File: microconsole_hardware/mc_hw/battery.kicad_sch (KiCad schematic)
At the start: 25 parts, among them J2 USB_C_Receptacle, Q1 DMP2035U-7, Q2 DMP2035U-7, SW19 SPDT_Slide_PTH_11.6x4.0mm, U1 MCP73833-FCI/UN, U2 S2B-PH-K-S

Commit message: second cleanup
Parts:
- removed C1, C2: 10uF, project_parts:C_0805_2012Metric_KEMET_IPC-B, symbol Device:C
- added C26, C27: 1206ZD106KAT2A, project_parts:C1206, symbol project_parts:1206ZD106KAT2A
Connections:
- net BAT+: now also C27.2
- net GND: now also C26.1, C27.1
- net USB-VBUS: now also C26.2

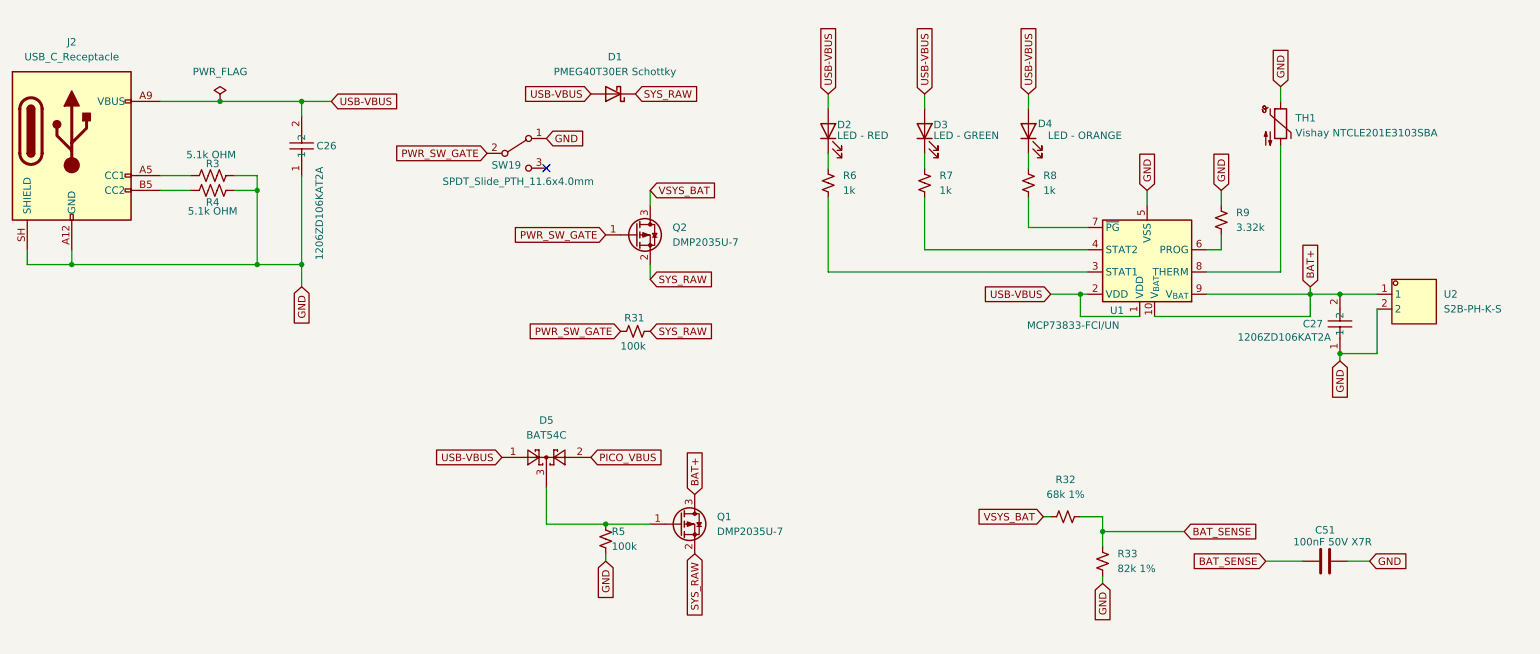
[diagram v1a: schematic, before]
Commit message: resistor and capacitor consolidation.
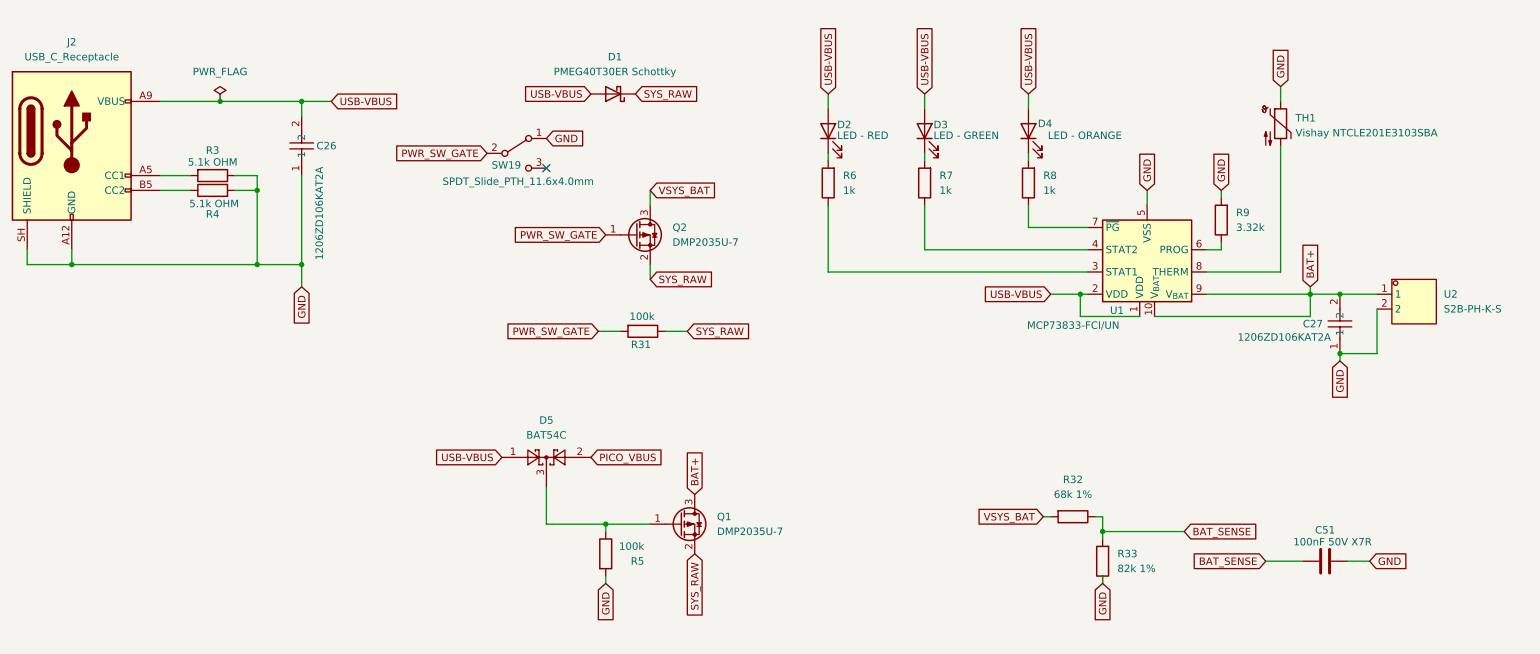
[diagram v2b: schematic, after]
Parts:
- R3, R4: footprint PCM_SparkFun-Resistor:R_0603_1608Metric -> Resistor_SMD:R_0603_1608Metric; symbol PCM_SparkFun-Resistor:R -> Device:R
- R31, R32, R33, R5, R6, R7, R8, R9: footprint PCM_SparkFun-Resistor:R_0603_1608Metric -> Resistor_SMD:R_0603_1608Metric; symbol PCM_SparkFun-Resistor:0.47_0603 -> Device:R
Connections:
- net GND: now also R3.1, R4.2; no longer R3.2, R4.1
- net at J2.A5 (CC1): now also R3.2; no longer R3.1
- net at J2.B5 (CC2): now also R4.1; no longer R4.2

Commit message: cleanup caps and resistors
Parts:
- R3, R4: value 5.1k OHM -> 5.1k
- R32: value 68k 1% -> 68k
- R33: value 82k 1% -> 82k
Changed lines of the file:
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@@
 			)
 		)
-		(property "Value" "68k 1%"
+		(property "Value" "68k"
 			(at 199.39 106.68 90)
 			(show_name no)
@@
 			)
 		)
-		(property "Value" "5.1k OHM"
+		(property "Value" "5.1k"
 			(at 52.07 49.784 90)
 			(show_name no)
@@
 			)
 		)
-		(property "Value" "5.1k OHM"
+		(property "Value" "5.1k"
 			(at 52.324 56.896 90)
 			(show_name no)
@@
 			)
 		)
-		(property "Value" "82k 1%"
+		(property "Value" "82k"
 			(at 207.01 119.3799 0)
 			(show_name no)

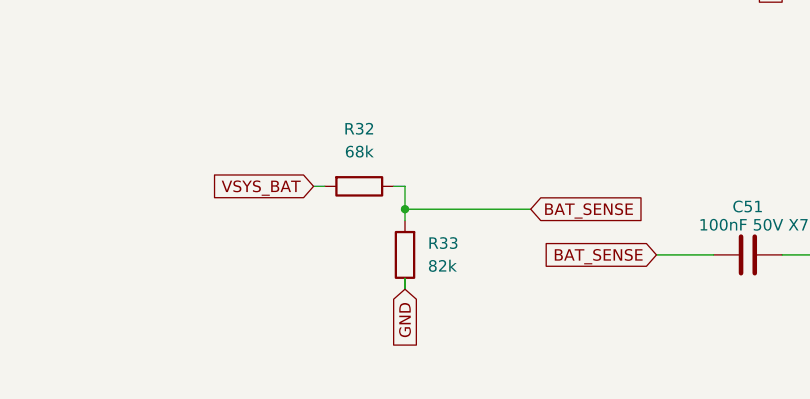
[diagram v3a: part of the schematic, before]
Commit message: cleanup ic symbol pin types
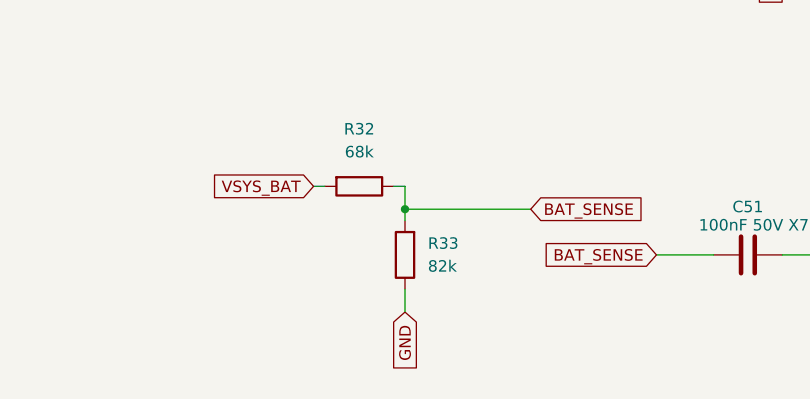
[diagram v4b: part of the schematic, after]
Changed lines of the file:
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@@
+	)
+	(junction
+		(at 204.47 113.03)
+		(diameter 0)
+		(color 0 0 0 0)
 	)
 	(junction
@@
 		(color 0 0 0 0)
 	)
-	(junction
-		(at 204.47 113.03)
-		(diameter 0)
-		(color 0 0 0 0)
-	)
 	(no_connect
 		(at 109.22 50.8)
@@
 	(wire
 		(pts
-			(xy 204.47 121.92) (xy 204.47 120.65)
-		)
-		(stroke
-			(width 0)
-			(type default)
-		)
-	)
-	(wire
-		(pts
 			(xy 173.99 49.53) (xy 173.99 48.26)
 		)
@@
 	(wire
 		(pts
+			(xy 204.47 113.03) (xy 218.44 113.03)
+		)
+		(stroke
+			(width 0)
+			(type default)
+		)
+	)
+	(wire
+		(pts
 			(xy 191.77 60.96) (xy 201.93 60.96)
 		)
@@
 	(wire
 		(pts
-			(xy 204.47 113.03) (xy 218.44 113.03)
-		)
-		(stroke
-			(width 0)
-			(type default)
-		)
-	)
-	(wire
-		(pts
 			(xy 232.41 118.11) (xy 238.76 118.11)
 		)
@@
 	(wire
 		(pts
+			(xy 204.47 113.03) (xy 204.47 114.3)
+		)
+		(stroke
+			(width 0)
+			(type default)
+		)
+	)
+	(wire
+		(pts
 			(xy 245.11 72.39) (xy 251.46 72.39)
 		)
@@
 	(wire
 		(pts
+			(xy 204.47 124.46) (xy 204.47 121.92)
+		)
+		(stroke
+			(width 0)
+			(type default)
+		)
+	)
+	(wire
+		(pts
 			(xy 173.99 38.1) (xy 173.99 40.64)
 		)
@@
 	(wire
 		(pts
-			(xy 204.47 110.49) (xy 204.47 114.3)
+			(xy 204.47 110.49) (xy 204.47 113.03)
 		)
 		(stroke
@@
 	(global_label "GND"
 		(shape input)
-		(at 204.47 121.92 270)
+		(at 204.47 124.46 270)
 		(fields_autoplaced yes)
 		(effects
@@
 		)
 		(property "Intersheetrefs" "${INTERSHEET_REFS}"
-			(at 204.47 128.7757 90)
-			(hide yes)
-			(show_name no)
+			(at 204.47 131.3157 90)
+			(hide yes)
+			(show_name no)

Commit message: consolidate parts 1
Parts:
- D2: MPN (none) -> LTST-C190KRKT; Manufacturer (none) -> Lite-On Inc.
- D3: MPN (none) -> LTST-C190KGKT; Manufacturer (none) -> Lite-On Inc.
- D4: MPN (none) -> LTST-C190KFKT; Manufacturer (none) -> Lite-On Inc.
- Q1, Q2: footprint (none) -> Package_TO_SOT_SMD:SOT-23
- R3, R4: MPN (none) -> RC0603FR-075K1L; Manufacturer (none) -> YAGEO; Power (none) -> 0.1W; Tolerance (none) -> 1%
- R31, R5: MPN (none) -> RC0603FR-07100KL; Manufacturer (none) -> YAGEO; Power (none) -> 0.1W; Tolerance (none) -> 1%
- R32: MPN (none) -> RC0603FR-0768KL; Manufacturer (none) -> YAGEO; Power (none) -> 0.1W; Tolerance (none) -> 1%
- R33: MPN (none) -> RC0603FR-0782KL; Manufacturer (none) -> YAGEO; Power (none) -> 0.1W; Tolerance (none) -> 1%
- R6, R7, R8: MPN (none) -> RC0603FR-071KL; Manufacturer (none) -> YAGEO; Power (none) -> 0.1W; Tolerance (none) -> 1%
- R9: MPN (none) -> RC0603FR-073K32L; Manufacturer (none) -> YAGEO; Power (none) -> 0.1W; Tolerance (none) -> 1%

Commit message: smal fix
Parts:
- Q1, Q2: MPN (none) -> DMP2035U-7; Manufacturer (none) -> Diodes Incorporated
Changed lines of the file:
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@@
+			)
+		)
+		(property "MPN" "DMP2035U-7"
+			(at 132.08 111.76 0)
+			(hide yes)
+			(show_name no)
+			(do_not_autoplace no)
+			(effects
+				(font
+					(size 1.27 1.27)
+				)
+			)
+		)
+		(property "Manufacturer" "Diodes Incorporated"
+			(at 132.08 111.76 0)
+			(hide yes)
+			(show_name no)
+			(do_not_autoplace no)
+			(effects
+				(font
+					(size 1.27 1.27)
+				)
 			)
 		)
@@
 			(at 124.46 62.23 0)
 			(hide yes)
+			(show_name no)
+			(do_not_autoplace no)
+			(effects
+				(font
+					(size 1.27 1.27)
+				)
+			)
+		)
+		(property "MPN" "DMP2035U-7"
+			(at 124.46 62.23 0)
+			(hide yes)
+			(show_name no)
+			(do_not_autoplace no)
+			(effects
+				(font
+					(size 1.27 1.27)
+				)
+			)
+		)
+		(property "Manufacturer" "Diodes Incorporated"
+			(at 124.46 62.23 0)
+			(hide yes)

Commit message: second fix
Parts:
- D1: MPN (none) -> PMEG40T30ERX; Manufacturer (none) -> Nexperia
- D5: MPN (none) -> BAT54C-7-F; Manufacturer (none) -> Diodes Incorporated
- SW19: MPN (none) -> COM-00102; Manufacturer (none) -> SparkFun Electronics
- TH1: MPN (none) -> NTCLE201E3103SBA; Manufacturer (none) -> Vishay / BCcomponents
- U1: MPN (none) -> MCP73833-FCI/UN; Manufacturer (none) -> Microchip Technology
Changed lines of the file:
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@@
+			)
+		)
+		(property "MPN" "PMEG40T30ERX"
+			(at 120.65 38.1 0)
+			(hide yes)
+			(show_name no)
+			(do_not_autoplace no)
+			(effects
+				(font
+					(size 1.27 1.27)
+				)
+			)
+		)
+		(property "Manufacturer" "Nexperia"
+			(at 120.65 38.1 0)
+			(hide yes)
+			(show_name no)
+			(do_not_autoplace no)
+			(effects
+				(font
+					(size 1.27 1.27)
+				)
 			)
 		)
@@
 			)
 		)
+		(property "MPN" "MCP73833-FCI/UN"
+			(at 212.09 63.5 0)
+			(hide yes)
+			(show_name no)
+			(do_not_autoplace no)
+			(effects
+				(font
+					(size 1.27 1.27)
+				)
+			)
+		)
+		(property "Manufacturer" "Microchip Technology"
+			(at 212.09 63.5 0)
+			(hide yes)
+			(show_name no)
+			(do_not_autoplace no)
+			(effects
+				(font
+					(size 1.27 1.27)
+				)
+			)
+		)
 		(pin "6"
 		)
@@
 			)
 		)
+		(property "MPN" "COM-00102"
+			(at 104.14 48.26 0)
+			(hide yes)
+			(show_name no)
+			(do_not_autoplace no)
+			(effects
+				(font
+					(size 1.27 1.27)
+				)
+			)
+		)
+		(property "Manufacturer" "SparkFun Electronics"
+			(at 104.14 48.26 0)
+			(hide yes)
+			(show_name no)
+			(do_not_autoplace no)
+			(effects
+				(font
+					(size 1.27 1.27)
+				)
+			)
+		)
 		(pin "2"
 		)
@@
 			)
 		)
+		(property "MPN" "BAT54C-7-F"
+			(at 109.22 100.33 0)
+			(hide yes)
+			(show_name no)
+			(do_not_autoplace no)
+			(effects
+				(font
+					(size 1.27 1.27)
+				)
+			)
+		)
+		(property "Manufacturer" "Diodes Incorporated"
+			(at 109.22 100.33 0)
+			(hide yes)
+			(show_name no)
+			(do_not_autoplace no)
+			(effects
+				(font
+					(size 1.27 1.27)
+				)
+			)
+		)
 		(pin "2"
 		)
@@
 			(at 234.95 43.18 0)
 			(hide yes)
+			(show_name no)
+			(do_not_autoplace no)
+			(effects
+				(font
+					(size 1.27 1.27)
+				)
+			)
+		)
+		(property "MPN" "NTCLE201E3103SBA"
+			(at 234.95 43.18 0)
+			(hide yes)
+			(show_name no)
+			(do_not_autoplace no)
+			(effects
+				(font
+					(size 1.27 1.27)
+				)
+			)
+		)
+		(property "Manufacturer" "Vishay / BCcomponents"
+			(at 234.95 43.18 0)
+			(hide yes)

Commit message: bom cleanup
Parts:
- C26, C27: Tolerance (none) -> 10%; Voltage (none) -> 10V
- C51: Tolerance (none) -> 10%; Voltage (none) -> 50V
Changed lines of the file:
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@@
+			)
+		)
+		(property "Tolerance" "10%"
+			(at 242.57 118.11 90)
+			(hide yes)
+			(show_name no)
+			(do_not_autoplace no)
+			(effects
+				(font
+					(size 1.27 1.27)
+				)
+			)
+		)
+		(property "Voltage" "50V"
+			(at 242.57 118.11 90)
+			(hide yes)
+			(show_name no)
+			(do_not_autoplace no)
+			(effects
+				(font
+					(size 1.27 1.27)
+				)
 			)
 		)
@@
 			)
 		)
-		(property "Datasheet" "https://lcsc.com/product-detail/presales_AVX-1206ZD106KAT2A_C597553.html"
+		(property "Datasheet" ""
 			(at 255.27 77.47 0)
 			(hide yes)
@@
 		)
 		(property "Power" ""
+			(at 245.11 77.47 90)
+			(hide yes)
+			(show_name no)
+			(do_not_autoplace no)
+			(effects
+				(font
+					(size 1.27 1.27)
+				)
+			)
+		)
+		(property "Tolerance" "10%"
+			(at 245.11 77.47 90)
+			(hide yes)
+			(show_name no)
+			(do_not_autoplace no)
+			(effects
+				(font
+					(size 1.27 1.27)
+				)
+			)
+		)
+		(property "Voltage" "10V"
 			(at 245.11 77.47 90)
 			(hide yes)
@@
 			)
 		)
-		(property "Datasheet" "https://lcsc.com/product-detail/presales_AVX-1206ZD106KAT2A_C597553.html"
+		(property "Datasheet" ""
 			(at 77.47 46.99 0)
 			(hide yes)
@@
 			(at 67.31 46.99 90)
 			(hide yes)
+			(show_name no)
+			(do_not_autoplace no)
+			(effects
+				(font
+					(size 1.27 1.27)
+				)
+			)
+		)
+		(property "Tolerance" "10%"
+			(at 67.31 46.99 90)
+			(hide yes)
+			(show_name no)
+			(do_not_autoplace no)
+			(effects
+				(font
+					(size 1.27 1.27)
+				)
+			)
+		)
+		(property "Voltage" "10V"
+			(at 67.31 46.99 90)
+			(hide yes)
